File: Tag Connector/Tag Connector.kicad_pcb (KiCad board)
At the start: 2 copper layers, 44.3 x 25 mm, 7 parts, among them J1 Conn_01x05_Male, J2 Conn_01x05_Male

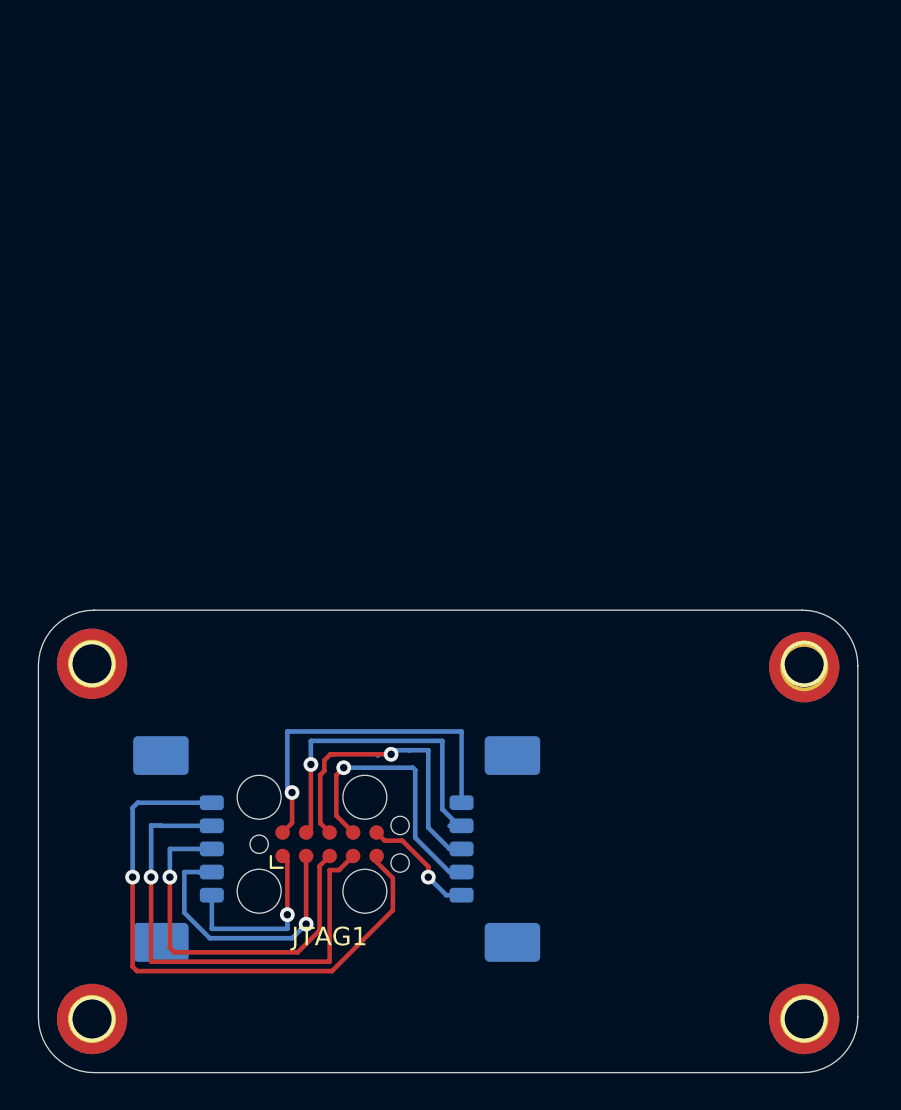
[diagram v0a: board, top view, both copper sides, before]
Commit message: updated manufacturing files
used correct dxf file to adjust the mounting holes on the PCB
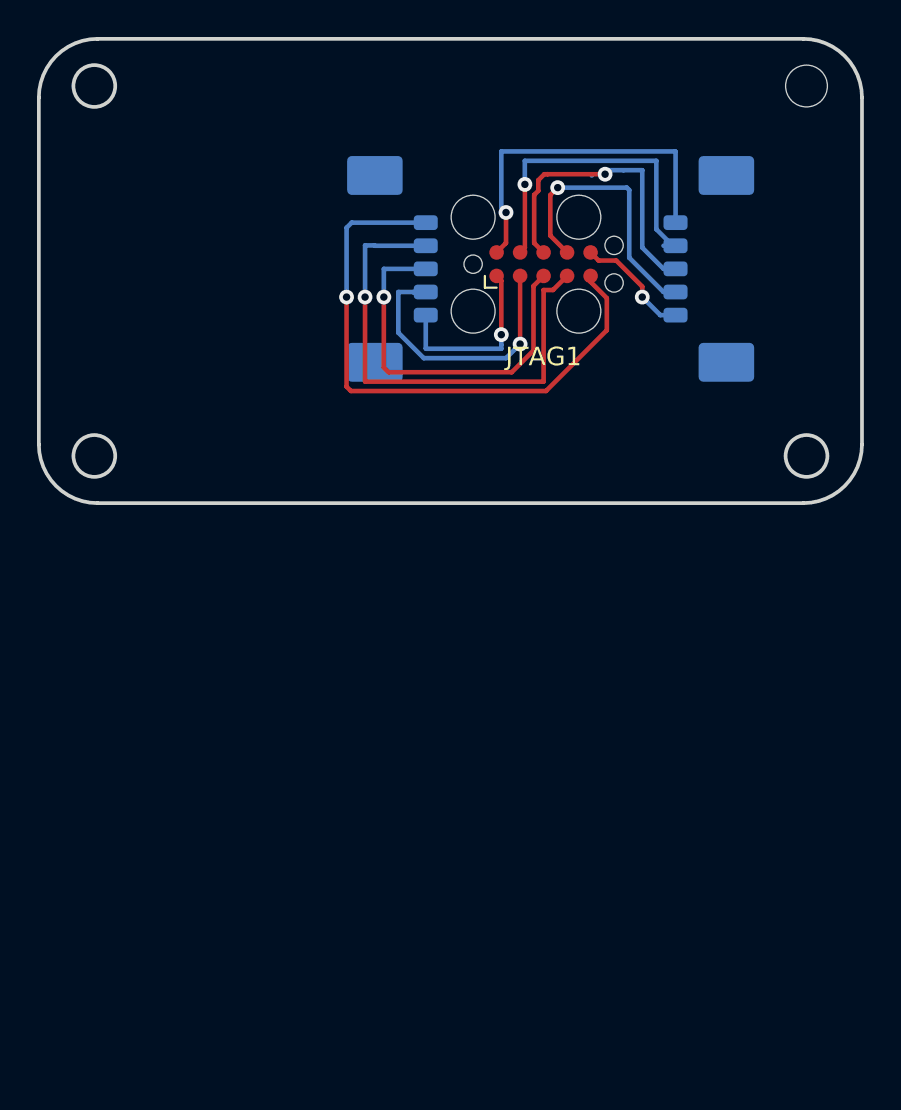
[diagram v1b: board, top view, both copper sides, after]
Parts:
- removed REF** (x4): MountingHole_2.2mm_M2_DIN965_Pad_TopBottom, MountingHole:MountingHole_2.2mm_M2_DIN965_Pad_TopBottom
- moved J1 33.4 mm to (153.6, 67.4)
- moved J2 33.4 mm to (169.6, 67.4)
- moved JTAG1 33.4 mm to (161.2, 67.2)
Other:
- board size 44.3 x 25 mm -> 44.5 x 25.1 mm

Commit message: Create v3 flight computer
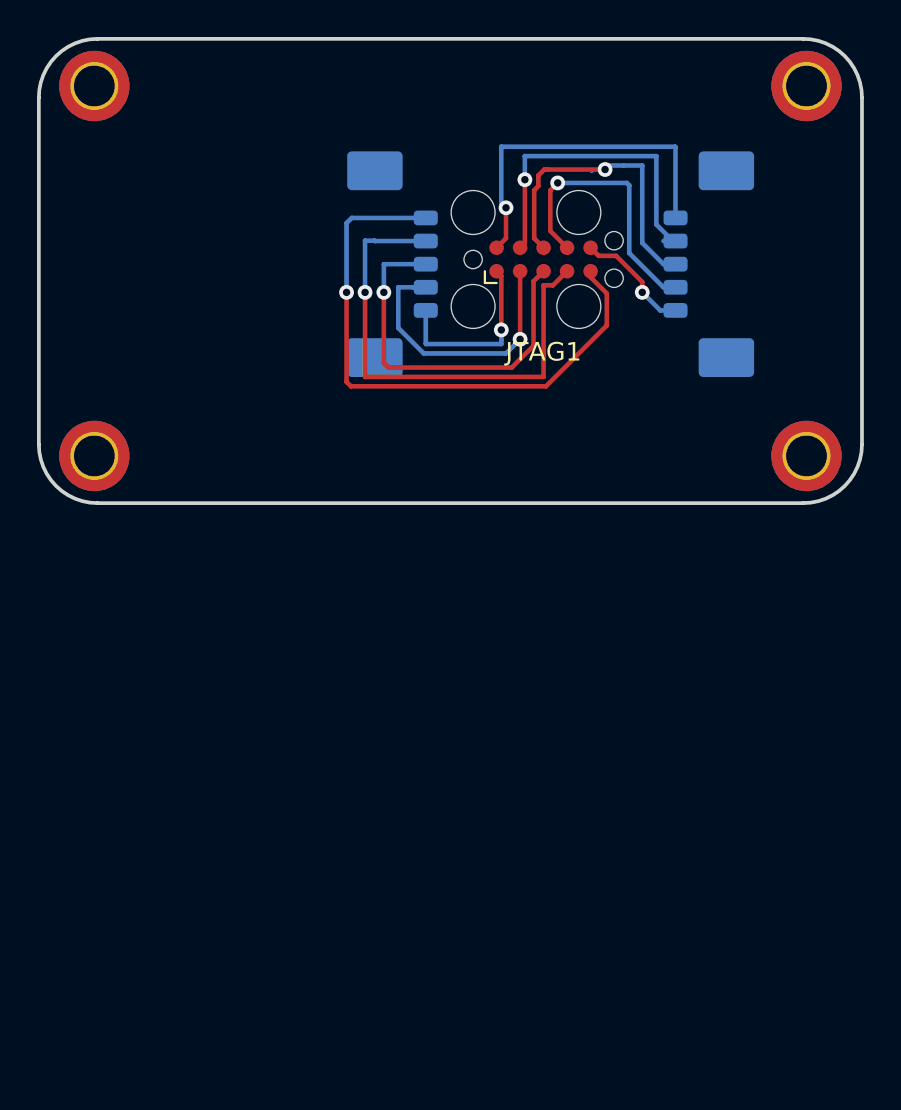
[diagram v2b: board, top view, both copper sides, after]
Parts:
- added ?: MountingHole_2.2mm_M2_DIN965_Pad_TopBottom, MountingHole:MountingHole_2.2mm_M2_DIN965_Pad_TopBottom, F.Cu at (136.9, 57.6)
- added REF**: MountingHole_2.2mm_M2_DIN965_Pad_TopBottom, MountingHole:MountingHole_2.2mm_M2_DIN965_Pad_TopBottom, F.Cu at (175.4, 77.6)
- added REF**: MountingHole_2.2mm_M2_DIN965_Pad_TopBottom, MountingHole:MountingHole_2.2mm_M2_DIN965_Pad_TopBottom, F.Cu at (175.4, 57.6)
- added REF**: MountingHole_2.2mm_M2_DIN965_Pad_TopBottom, MountingHole:MountingHole_2.2mm_M2_DIN965_Pad_TopBottom, F.Cu at (136.9, 77.6)
- moved JTAG1 0.25 mm to (161.2, 66.9)
- moved J1 0.25 mm to (153.6, 67.2)
- moved J2 0.25 mm to (169.6, 67.2)
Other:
- outline, holes or cut-outs redrawn
